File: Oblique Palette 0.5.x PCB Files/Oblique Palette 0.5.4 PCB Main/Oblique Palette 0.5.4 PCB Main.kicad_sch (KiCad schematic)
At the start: 6 parts, among them U1 CD4051B, U2 Pico

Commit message: Associated Input and Output tiles relatively rather than absolutely, which got them lost in the sauce.
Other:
- sheet Input 1: file ../../Oblique Palette 0.5.1 PCB Input/Oblique Palette 0.5.1 PCB Input.kicad_sch -> ../Oblique Palette 0.5.1 PCB Input/Oblique Palette 0.5.1 PCB Input.kicad_sch
- sheet Output1: file ../../Oblique Palette 0.5.1 PCB Output/Oblique Palette 0.5.1 PCB Output.kicad_sch -> ../Oblique Palette 0.5.1 PCB Output/Oblique Palette 0.5.1 PCB Output.kicad_sch
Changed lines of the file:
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@@
 			)
 		)
-		(property "Sheetfile" "../../Oblique Palette 0.5.1 PCB Output/Oblique Palette 0.5.1 PCB Output.kicad_sch"
+		(property "Sheetfile" "../Oblique Palette 0.5.1 PCB Output/Oblique Palette 0.5.1 PCB Output.kicad_sch"
 			(at 38.6846 123.19 90)
 			(effects
@@
 			)
 		)
-		(property "Sheetfile" "../../Oblique Palette 0.5.1 PCB Input/Oblique Palette 0.5.1 PCB Input.kicad_sch"
+		(property "Sheetfile" "../Oblique Palette 0.5.1 PCB Input/Oblique Palette 0.5.1 PCB Input.kicad_sch"
 			(at 13.97 59.0046 0)
 			(effects

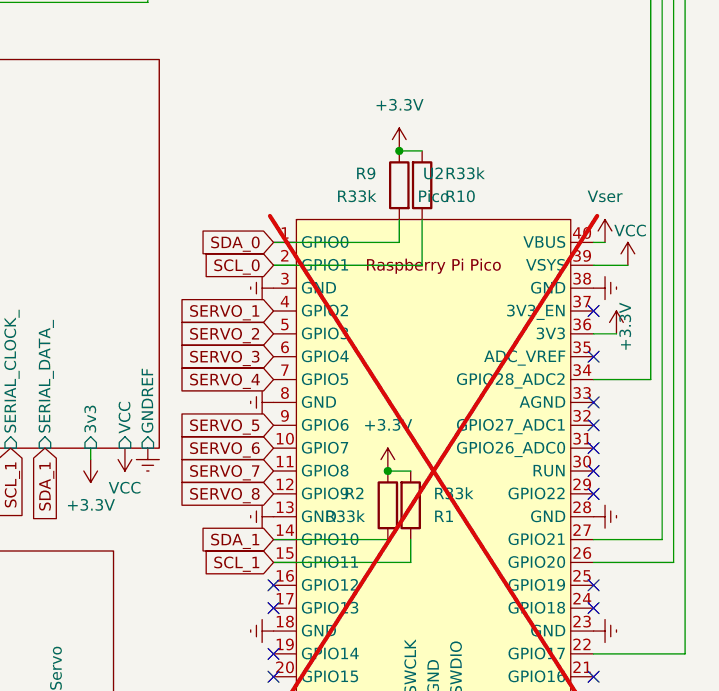
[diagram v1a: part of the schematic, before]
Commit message: Hunting for bugs between Linux and Mac
Palette works fine on Mac, though with a 40Hz sample rate.

Palette works in Linux with a 340Hz sample rate but suddenly stops after a random number of seconds. It does *not* go down to a sample rate of 0.25 as it was doing before. The microcontroller just completely stops at a certain point in the process.
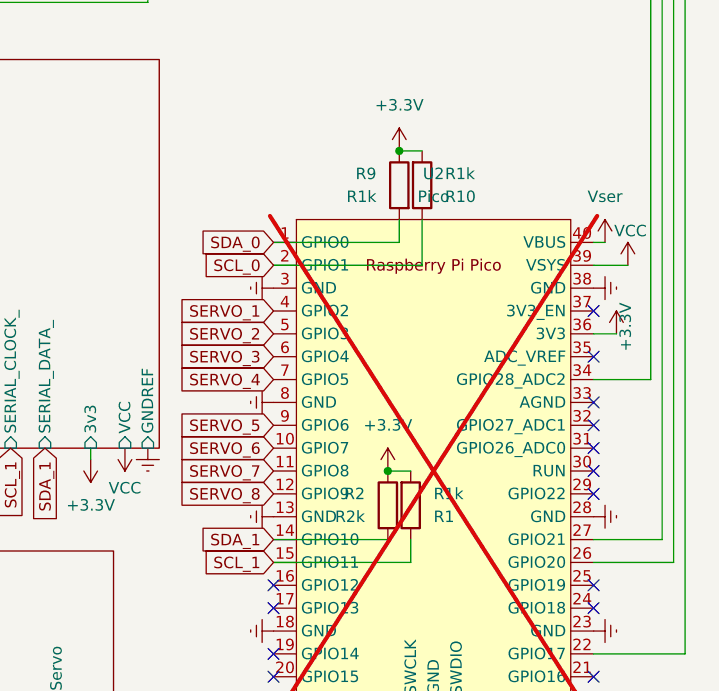
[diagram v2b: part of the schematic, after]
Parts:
- R1, R10, R9: value R33k -> R1k
- R2: value R33k -> R2k
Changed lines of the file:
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@@
 			)
 		)
-		(property "Value" "R33k"
+		(property "Value" "R1k"
 			(at 256.54 92.7101 0)
 			(effects
@@
 			)
 		)
-		(property "Value" "R33k"
+		(property "Value" "R2k"
 			(at 247.65 130.8099 0)
 			(effects
@@
 			)
 		)
-		(property "Value" "R33k"
+		(property "Value" "R1k"
 			(at 248.92 95.2499 0)
 			(effects
@@
 			)
 		)
-		(property "Value" "R33k"
+		(property "Value" "R1k"
 			(at 255.27 128.2701 0)
 			(effects
